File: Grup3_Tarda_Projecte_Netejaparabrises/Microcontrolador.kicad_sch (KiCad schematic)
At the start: 21 parts, among them IC1 PIC18F258-I_SO, J13 FINAL DE CARRERA, J2 BOTONERA, J3 PROGRAMMING CON, J5 DE9_Plug_MountingHoles, J5 JP1, J6 DE9_Plug_MountingHoles, SW1 SW_Push, U1 TCAN1042DRQ1, Y1 ABLS2-8.000MHZ-D4Y-T

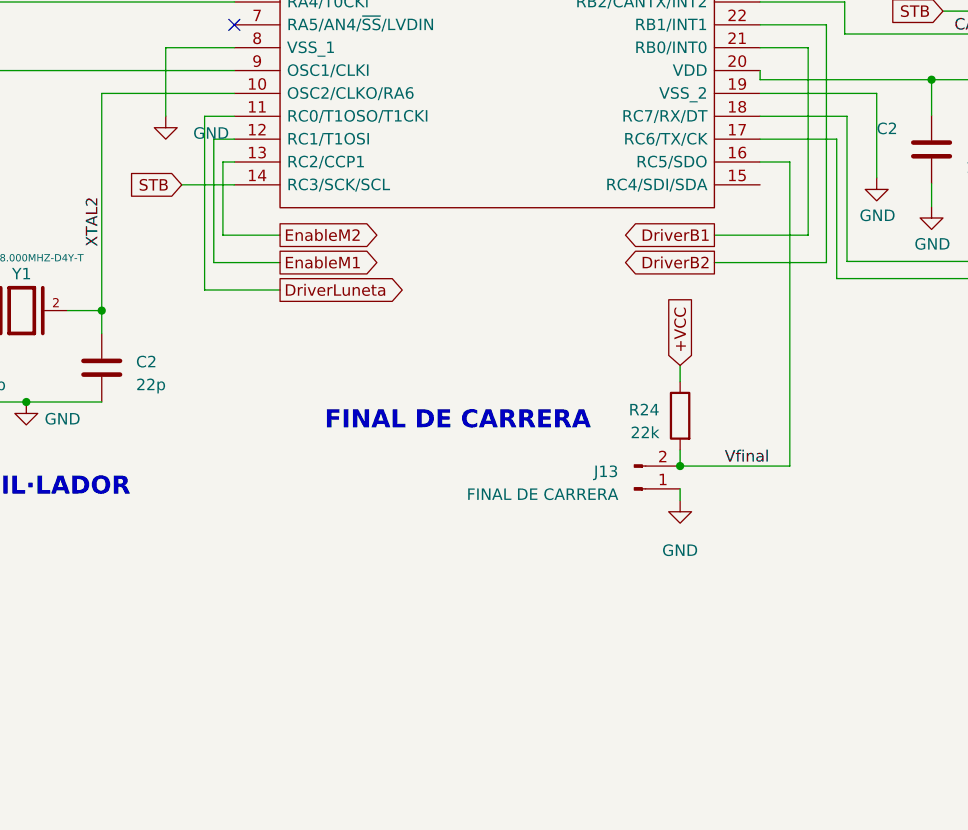
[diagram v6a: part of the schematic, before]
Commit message: afegits els finals de carrera dels motors
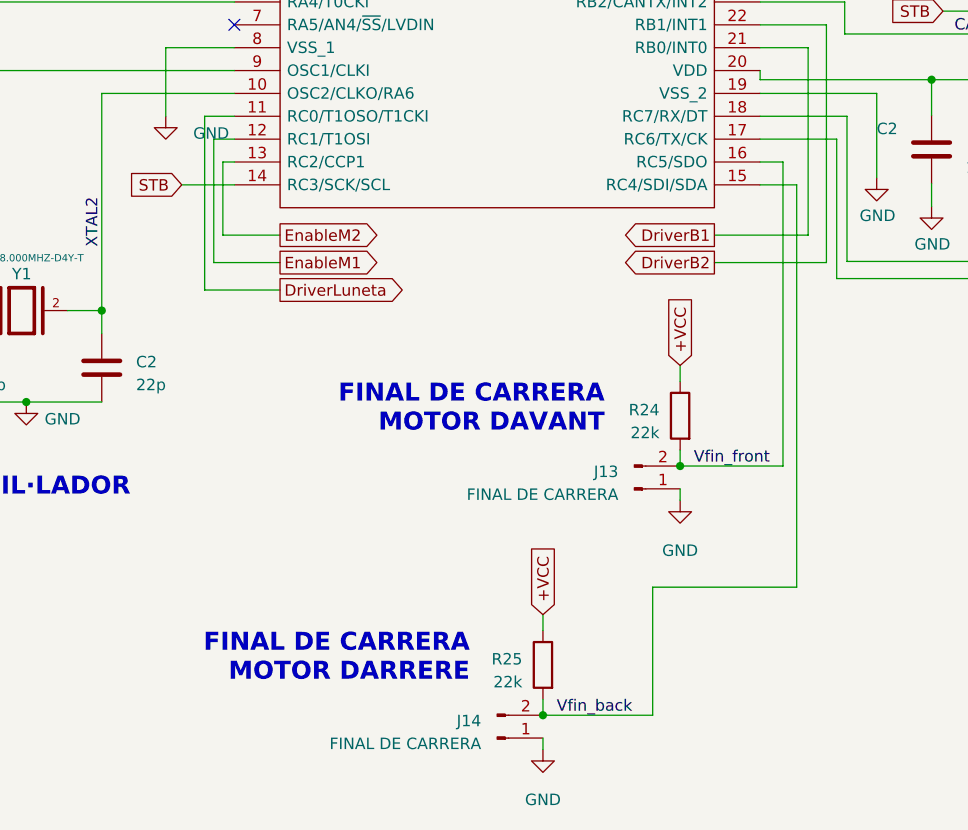
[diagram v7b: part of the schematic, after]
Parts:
- added J14: FINAL DE CARRERA, Connector_PinSocket_1.00mm:PinSocket_1x02_P1.00mm_Vertical, symbol Connector:Conn_01x02_Pin
- added R25: 22k, Resistor_SMD:R_0805_2012Metric_Pad1.20x1.40mm_HandSolder, symbol Device:R
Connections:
- net +VCC: now also R25.1
- net GND: now also J14.1 (Pin_1)
- net Vfin_back: now reaches IC1.15 (RC4/SDI/SDA)
- net Vfin_back: now also J14.2 (Pin_2), R25.2
- net Vfinal renamed Vfin_front
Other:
- note added: "FINAL DE CARRERA MOTOR DARRERE"
- note added: "FINAL DE CARRERA MOTOR DAVANT"
- note removed: "FINAL DE CARRERA"
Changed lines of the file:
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@@
   (junction (at 44.704 123.444) (diameter 0) (color 0 0 0 0)
+  )
+  (junction (at 149.352 173.482) (diameter 0) (color 0 0 0 0)
   )
   (junction (at 100.33 128.524) (diameter 0) (color 0 0 0 0)
@@
   (no_connect (at 203.708 100.33))
   (no_connect (at 221.996 146.558))
-  (wire (pts (xy 164.592 145.796) (xy 176.784 145.796))
+  (wire (pts (xy 164.592 145.796) (xy 176.022 145.796))
     (stroke (width 0) (type default))
   )
@@
     (stroke (width 0) (type default))
   )
+  (wire (pts (xy 149.352 162.306) (xy 149.352 164.084))
+    (stroke (width 0) (type default))
+  )
   (wire (pts (xy 21.082 112.014) (xy 35.814 112.014))
     (stroke (width 0) (type default))
@@
     (stroke (width 0) (type default))
   )
+  (wire (pts (xy 149.352 173.482) (xy 161.544 173.482))
+    (stroke (width 0) (type default))
+  )
   (wire (pts (xy 44.704 132.334) (xy 47.498 132.334))
     (stroke (width 0) (type default))
   )
+  (wire (pts (xy 149.352 176.022) (xy 149.352 177.292))
+    (stroke (width 0) (type default))
+  )
   (wire (pts (xy 44.704 143.764) (xy 61.214 143.764))
     (stroke (width 0) (type default))
@@
     (stroke (width 0) (type default))
   )
+  (wire (pts (xy 161.544 173.482) (xy 161.544 159.258))
+    (stroke (width 0) (type default))
+  )
   (wire (pts (xy 37.084 56.896) (xy 37.084 59.436))
     (stroke (width 0) (type default))
@@
     (stroke (width 0) (type default))
   )
+  (wire (pts (xy 177.546 159.258) (xy 177.546 114.554))
+    (stroke (width 0) (type default))
+  )
   (wire (pts (xy 47.498 114.554) (xy 47.498 132.334))
     (stroke (width 0) (type default))
@@
     (stroke (width 0) (type default))
   )
-  (wire (pts (xy 176.784 145.796) (xy 176.784 112.014))
+  (wire (pts (xy 176.022 145.796) (xy 176.022 112.014))
     (stroke (width 0) (type default))
   )
@@
     (stroke (width 0) (type default))
   )
-  (wire (pts (xy 176.784 112.014) (xy 173.482 112.014))
+  (wire (pts (xy 149.352 171.704) (xy 149.352 173.482))
+    (stroke (width 0) (type default))
+  )
+  (wire (pts (xy 176.022 112.014) (xy 173.482 112.014))
     (stroke (width 0) (type default))
   )
@@
   )
   (wire (pts (xy 31.75 161.544) (xy 31.75 114.554))
+    (stroke (width 0) (type default))
+  )
+  (wire (pts (xy 177.546 114.554) (xy 173.482 114.554))
+    (stroke (width 0) (type default))
+  )
+  (wire (pts (xy 161.544 159.258) (xy 177.546 159.258))
     (stroke (width 0) (type default))
   )
@@
     (effects (font (size 3 3) (thickness 0.6) bold) (justify left bottom))
   )
-  (text "FINAL DE CARRERA" (at 154.686 141.986 0)
+  (text "FINAL DE CARRERA\nMOTOR DAVANT" (at 156.21 142.24 0)
+    (effects (font (size 2 2) (thickness 0.6) bold) (justify right bottom))
+  )
+  (text "FINAL DE CARRERA\nMOTOR DARRERE" (at 141.224 169.926 0)
     (effects (font (size 2 2) (thickness 0.6) bold) (justify right bottom))
   )
@@
     (effects (font (size 1.27 1.27)) (justify left bottom))
   )
-  (label "Vfinal" (at 174.498 145.796 180) (fields_autoplaced)
-    (effects (font (size 1.27 1.27)) (justify right bottom))
+  (label "Vfin_front" (at 166.116 145.796 0) (fields_autoplaced)
+    (effects (font (size 1.27 1.27)) (justify left bottom))
   )
   (label "XTAL1" (at 82.804 121.412 90) (fields_autoplaced)
@@
   )
   (label "Rx" (at 218.948 144.018 0) (fields_autoplaced)
+    (effects (font (size 1.27 1.27)) (justify left bottom))
+  )
+  (label "Vfin_back" (at 150.876 173.482 0) (fields_autoplaced)
     (effects (font (size 1.27 1.27)) (justify left bottom))
   )
@@
     )
   )
+  (global_label "+VCC" (shape input) (at 149.352 162.306 90) (fields_autoplaced)
+    (effects (font (size 1.27 1.27)) (justify left))
+    (property "Intersheetrefs" "${INTERSHEET_REFS}" (at 149.352 154.1992 90)
+      (effects (font (size 1.27 1.27)) (justify right) hide)
+    )
+  )
   (symbol (lib_id "power:GND") (at 34.544 68.326 0) (unit 1)
     (in_bom yes) (on_board yes) (dnp no) (fields_autoplaced)
@@
         (path "/f9f603a9-b774-48a7-94d1-4c8d3d65a3f8"
           (reference "#PWR017") (unit 1)
+        )
+      )
+    )
+  )
+  (symbol (lib_id "power:GND") (at 149.352 177.292 0) (mirror y) (unit 1)
+    (in_bom yes) (on_board yes) (dnp no) (fields_autoplaced)
+    (property "Reference" "#PWR045" (at 149.352 183.642 0)
+      (effects (font (size 1.27 1.27)) hide)
+    )
+    (property "Value" "GND" (at 149.352 182.88 0)
+      (effects (font (size 1.27 1.27)))
+    )
+    (property "Footprint" "" (at 149.352 177.292 0)
+      (effects (font (size 1.27 1.27)) hide)
+    )
+    (property "Datasheet" "" (at 149.352 177.292 0)
+      (effects (font (size 1.27 1.27)) hide)
+    )
+    (pin "1")
+    (instances
+      (project "Grup3_Tarda_Projecte_Netejaparabrises"
+        (path "/7ae78f34-680b-4fd9-8391-ce3e1c73c4b5/41ec4c6b-5222-4808-bf2f-f72f20229182"
+          (reference "#PWR045") (unit 1)
         )
       )
@@
     )
   )
+  (symbol (lib_id "Connector:Conn_01x02_Pin") (at 144.272 176.022 0) (mirror x) (unit 1)
+    (in_bom yes) (on_board yes) (dnp no) (fields_autoplaced)
+    (property "Reference" "J14" (at 142.494 174.117 0)
+      (effects (font (size 1.27 1.27)) (justify right))
+    )
+    (property "Value" "FINAL DE CARRERA" (at 142.494 176.657 0)
+      (effects (font (size 1.27 1.27)) (justify right))
+    )
+    (property "Footprint" "Connector_PinSocket_1.00mm:PinSocket_1x02_P1.00mm_Vertical" (at 144.272 176.022 0)
+      (effects (font (size 1.27 1.27)) hide)
+    )
+    (property "Datasheet" "~" (at 144.272 176.022 0)
+      (effects (font (size 1.27 1.27)) hide)
+    )
+    (pin "1")
+    (pin "2")
+    (instances
+      (project "Grup3_Tarda_Projecte_Netejaparabrises"
+        (path "/7ae78f34-680b-4fd9-8391-ce3e1c73c4b5/41ec4c6b-5222-4808-bf2f-f72f20229182"
+          (reference "J14") (unit 1)
+        )
+      )
+    )
+  )
   (symbol (lib_id "Device:R") (at 44.704 119.634 0) (unit 1)
     (in_bom yes) (on_board yes) (dnp no)
@@
         )
       )
+    )
+  )
+  (symbol (lib_id "Device:R") (at 149.352 167.894 0) (mirror y) (unit 1)
+    (in_bom yes) (on_board yes) (dnp no) (fields_autoplaced)
+    (property "Reference" "R25" (at 147.066 167.259 0)
+      (effects (font (size 1.27 1.27)) (justify left))
+    )
+    (property "Value" "22k" (at 147.066 169.799 0)
+      (effects (font (size 1.27 1.27)) (justify left))
+    )
+    (property "Footprint" "Resistor_SMD:R_0805_2012Metric_Pad1.20x1.40mm_HandSolder" (at 151.13 167.894 90)
+      (effects (font (size 1.27 1.27)) hide)
+    )
+    (property "Datasheet" "~" (at 149.352 167.894 0)
+      (effects (font (size 1.27 1.27)) hide)
+    )
+    (pin "1")
+    (pin "2")
+    (instances
+      (project "Grup3_Tarda_Projecte_Netejaparabrises"
+        (path "/7ae78f34-680b-4fd9-8391-ce3e1c73c4b5/41ec4c6b-5222-4808-bf2f-f72f20229182"
+          (reference "R25") (unit 1)
+        )
+      )

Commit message: definitiu
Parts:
- J13, J14: footprint Connector_PinSocket_1.00mm:PinSocket_1x02_P1.00mm_Vertical -> Connector_PinHeader_2.54mm:PinHeader_1x02_P2.54mm_Vertical
- J2: footprint Connector_PinSocket_2.54mm:PinSocket_1x06_P2.54mm_Vertical -> Connector_PinHeader_2.54mm:PinHeader_1x06_P2.54mm_Vertical
- J3: footprint Connector_PinSocket_2.54mm:PinSocket_1x05_P2.54mm_Vertical -> Connector_PinHeader_2.54mm:PinHeader_1x05_P2.54mm_Vertical
- J5: footprint Connector_PinSocket_2.54mm:PinSocket_1x03_P2.54mm_Vertical -> Connector_PinHeader_2.54mm:PinHeader_1x03_P2.54mm_Vertical
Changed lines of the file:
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@@
   (title_block
     (title "Projecte Netejaparabrises - Grup 4 Tarda")
-    (date "2023-04-20")
+    (date "2023-04-27")
     (rev "v1.3.20042023")
   )
@@
       (effects (font (size 1.27 1.27)) (justify right))
     )
-    (property "Footprint" "Connector_PinSocket_1.00mm:PinSocket_1x02_P1.00mm_Vertical" (at 144.272 176.022 0)
+    (property "Footprint" "Connector_PinHeader_2.54mm:PinHeader_1x02_P2.54mm_Vertical" (at 144.272 176.022 0)
       (effects (font (size 1.27 1.27)) hide)
     )
@@
       (effects (font (size 1.27 1.27)))
     )
-    (property "Footprint" "Connector_PinSocket_2.54mm:PinSocket_1x05_P2.54mm_Vertical" (at 34.544 51.816 0)
+    (property "Footprint" "Connector_PinHeader_2.54mm:PinHeader_1x05_P2.54mm_Vertical" (at 34.544 51.816 0)
       (effects (font (size 1.27 1.27)) hide)
     )
@@
       (effects (font (size 1.27 1.27)) (justify right))
     )
-    (property "Footprint" "Connector_PinSocket_1.00mm:PinSocket_1x02_P1.00mm_Vertical" (at 159.512 148.336 0)
+    (property "Footprint" "Connector_PinHeader_2.54mm:PinHeader_1x02_P2.54mm_Vertical" (at 159.512 148.336 0)
       (effects (font (size 1.27 1.27)) hide)
     )
@@
       (effects (font (size 1.27 1.27)))
     )
-    (property "Footprint" "Connector_PinSocket_2.54mm:PinSocket_1x06_P2.54mm_Vertical" (at 16.002 109.474 0)
+    (property "Footprint" "Connector_PinHeader_2.54mm:PinHeader_1x06_P2.54mm_Vertical" (at 16.002 109.474 0)
       (effects (font (size 1.27 1.27)) hide)
     )
@@
       (effects (font (size 1.27 1.27)))
     )
-    (property "Footprint" "Connector_PinSocket_2.54mm:PinSocket_1x03_P2.54mm_Vertical" (at 81.534 53.34 0)
-      (effects (font (size 1.27 1.27)) hide)
-    )
+    (property "Footprint" "Connector_PinHeader_2.54mm:PinHeader_1x03_P2.54mm_Vertical" (at 81.534 53.34 0)
+      (effects (font (size 1.27 1.27)) hide)
+    )
